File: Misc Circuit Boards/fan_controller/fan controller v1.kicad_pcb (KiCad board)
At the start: 2 copper layers, 40.6 x 21.9 mm, 52 parts, among them P1 AUX, P2 +12V Suppply, P3 Fan, P4 Fan, P5 Jumper, Q1 NPN, U1 Ocot

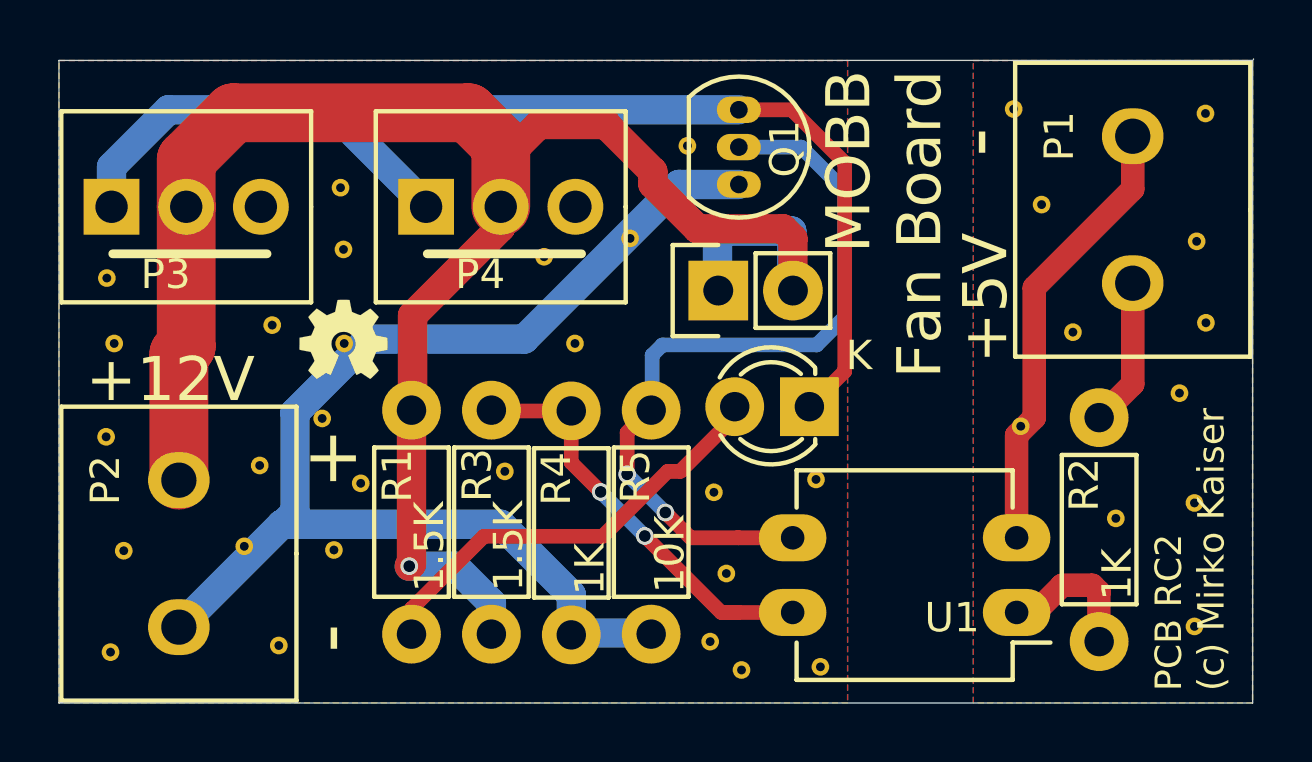
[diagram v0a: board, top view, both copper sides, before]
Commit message: * fan controller board RC3 - this should fix the LED jumper issue from RC2 * increased size of some solder pads * all GND now with thermal relieve * moved LED down by 0,5mm to make "CUT" area larger * added "no GND zone" around "CUT" area to give extra room
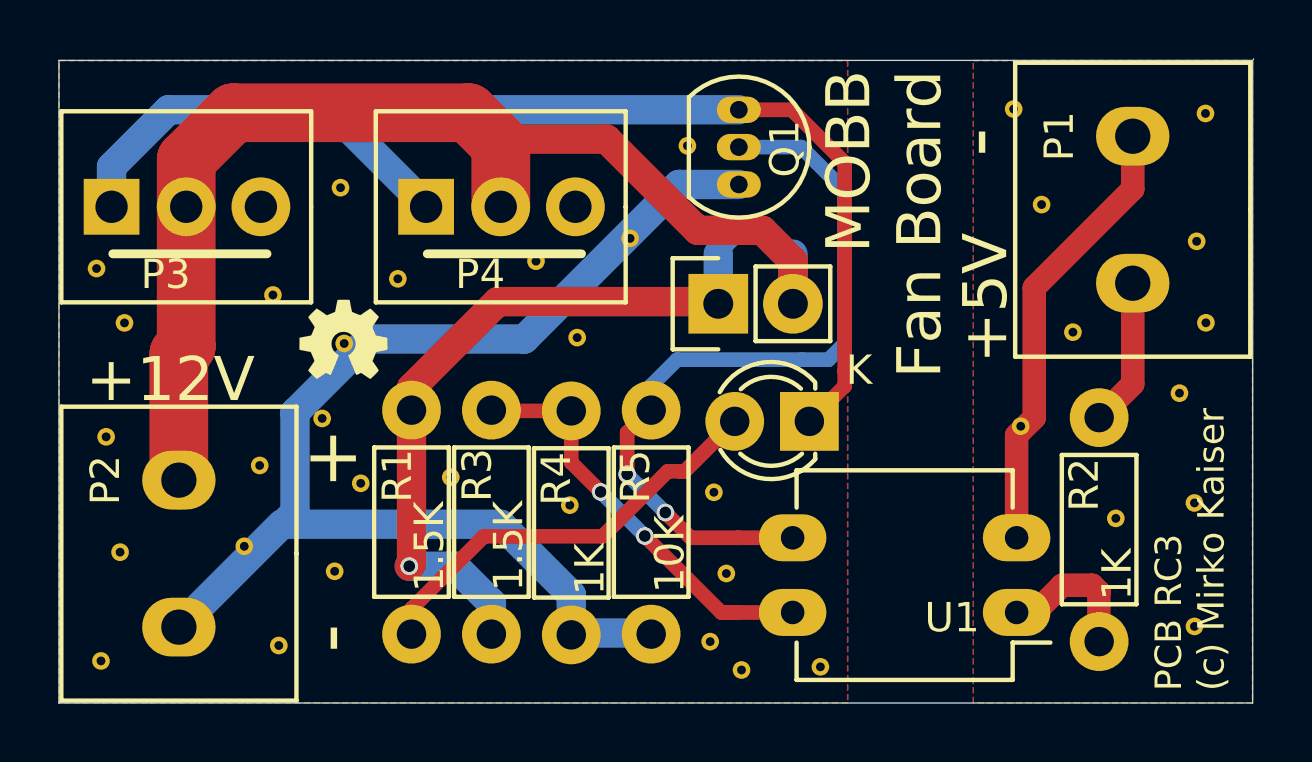
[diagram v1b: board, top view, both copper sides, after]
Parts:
- moved ? 8.42 mm to (201.6, 136.2)
- moved ? 2.10 mm to (195.7, 128.4)
- moved ? 1.85 mm to (197.5, 135.2)
- moved ? 1.03 mm to (191.4, 129.0)
- moved ? 0.78 mm to (186.4, 129.9)
- moved ? 0.73 mm to (193.6, 138.4)
- moved D1 0.50 mm to (209.7, 133.3)
- moved ? 0.48 mm to (185.4, 128.1)
- moved P5 0.45 mm to (206.6, 129.3)
- moved ? 0.44 mm to (185.6, 141.4)
- moved ? 0.31 mm to (200.4, 127.8)
- moved ? 0.21 mm to (201.8, 130.4)
- moved ? 0.13 mm to (186.2, 137.8)
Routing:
- net +12V: track 65.0 -> 66.8 mm
- net Net-(D1-Pad1): track 41.3 -> 41.8 mm
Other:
- board text added: "PCB RC3 (c) Mirko Kaiser"
- board text removed: "PCB RC2 (c) Mirko Kaiser"
